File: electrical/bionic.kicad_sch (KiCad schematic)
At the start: 22 parts, among them J1 GPIO, U1 CAT24C256

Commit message: add(electrical/symbol): Updated Components
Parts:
- removed C1: 100n, symbol Device:C_Small
- removed D? (x4): TB6612, symbol Motor_Driver:TB6612_DC_Driver
- removed J1: GPIO, Connector_PinSocket_2.54mm:PinSocket_2x20_P2.54mm_Vertical, symbol Connector_Generic:Conn_02x20_Odd_Even
- removed JP1: ID_WP, symbol Jumper:SolderJumper_2_Open
- removed M? (x8): N20, symbol bionic:N20_EN
- removed R1, R2: 3.9k, symbol Device:R_Small
- removed U1: CAT24C256, symbol Memory_EEPROM:CAT24C256
- removed U?: MCP23017, symbol bionic:MCP23017
- removed U?: CD4069, symbol bionic:CD4069
- removed U?: ESP32, symbol bionic:ESP32
- removed U?: ADS1115, symbol bionic:ADS1115
- added D1, D2, D3, D4: TB6612, symbol bionic:TB6612
- added M1, M2, M3, M4, M5, M6, M7: N20, symbol bionic:N20_EN
- added U1: ESP32, symbol bionic:ESP32
- added U2: SAMD09, symbol bionic:SAMD09
- added U3, U4: CD4069, symbol bionic:CD4069
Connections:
- net +3V3: now also D1.13 (STBY), D1.2 (VCC), D2.13 (STBY), D2.2 (VCC), D3.13 (STBY), D3.2 (VCC), D4.13 (STBY), D4.2 (VCC), M1.2 (VCC/BLK), M2.2 (VCC/BLK), M3.2 (VCC/BLK), M4.2 (VCC/BLK), M5.2 (VCC/BLK), M6.2 (VCC/BLK), M7.2 (VCC/BLK), U1.16 (VIN), U2.24 (VIN), U3.14 (VDD), U4.14 (VDD)
- net +6V: now also D1.1 (VM), D2.1 (VM), D3.1 (VM), D4.1 (VM)
- net EMG1: now also U2.1 (*2)
- net EMG2: now also U2.2 (*3)
- net GND: now also D1.3 (GND), D1.8 (GND), D1.9 (GND), D2.3 (GND), D2.8 (GND), D2.9 (GND), D3.3 (GND), D3.8 (GND), D3.9 (GND), D4.3 (GND), D4.8 (GND), D4.9 (GND), M1.5 (GND/BLU), M2.5 (GND/BLU), M3.5 (GND/BLU), M4.5 (GND/BLU), M5.5 (GND/BLU), M6.5 (GND/BLU), M7.5 (GND/BLU), U1.17 (GND), U2.22 (GND), U3.7 (GND), U4.7 (GND)
- net M1+: now also D1.4 (A01), M1.1 (M+/RED)
- net M1-: now also D1.5 (A02), M1.6 (M-/WHT)
- net M1B: now also D1.15 (AI2), U3.2 (A*)
- net M2+: now also D1.6 (B01), M2.1 (M+/RED)
- net M2-: now also D1.7 (B02), M2.6 (M-/WHT)
- net M2B: now also D1.11 (BI2), U3.4 (B*)
- net M3+: now also D2.4 (A01), M3.1 (M+/RED)
- net M3-: now also D2.5 (A02), M3.6 (M-/WHT)
- net M3B: now also D2.15 (AI2), U3.6 (C*)
- net M4+: now also D2.6 (B01), M4.1 (M+/RED)
- net M4-: now also D2.7 (B02), M4.6 (M-/WHT)
- net M4B: now also D2.11 (BI2), U3.8 (D*)
- net M5+: now also D3.4 (A01), M5.1 (M+/RED)
- net M5-: now also D3.5 (A02), M5.6 (M-/WHT)
- net M5B: now also D3.15 (AI2), U3.10 (*E)
- net M6+: now also D3.6 (B01), M6.1 (M+/RED)
- net M6-: now also D3.7 (B02), M6.6 (M-/WHT)
- net M6B: now also D3.11 (BI2), U3.12 (*F)
- net M7+: now also D4.4 (A01), M7.1 (M+/RED)
- net M7-: now also D4.5 (A02), M7.6 (M-/WHT)
- net M7B: now also D4.15 (AI2), U4.2 (A*)
- new net DIR1: D1.14 (AI1), U2.4 (~5), U3.1 (A)
- new net DIR2: D1.12 (BI1), U2.5 (~6), U3.3 (B)
- new net DIR3: D2.14 (AI1), U2.6 (~7), U3.5 (C)
- new net DIR4: D2.12 (BI1), U2.8 (9), U3.9 (D)
- new net DIR5: D3.14 (AI1), U2.9 (10), U3.11 (E)
- new net DIR6: D3.12 (BI1), U2.10 (11), U3.13 (F)
- new net DIR7: D4.14 (AI1), U2.11 (14), U4.1 (A)
- new net EMG3: U2.3 (*4)
- new net ENA1: M1.3 (A/YLW), U1.10 (IO19)
- new net ENA2: M2.3 (A/YLW), U1.18 (IO13)
- new net ENA3: M3.3 (A/YLW), U1.20 (IO14)
- new net ENA4: M4.3 (A/YLW), U1.22 (IO26)
- new net ENA5: M5.3 (A/YLW), U1.24 (IO33)
- new net ENA6: M6.3 (A/YLW), U1.26 (IO35)
- new net ENA7: M7.3 (A/YLW), U1.28 (IO39/VN)
- new net ENB1: M1.4 (B/GRN), U1.15 (IO23)
- new net ENB2: M2.4 (B/GRN), U1.19 (IO12*)
- new net ENB3: M3.4 (B/GRN), U1.21 (IO27)
- new net ENB4: M4.4 (B/GRN), U1.23 (IO25)
- new net ENB5: M5.4 (B/GRN), U1.25 (IO32)
- new net ENB6: M6.4 (B/GRN), U1.27 (IO34)
- new net ENB7: M7.4 (B/GRN), U1.29 (IO36/VP)
- new net PWM1: D1.16 (PWMA), U1.3 (IO15*)
- new net PWM2: D1.10 (PWMB), U1.4 (IO2*)
- new net PWM3: D2.16 (PWMA), U1.5 (IO4)
- new net PWM4: D2.10 (PWMB), U1.6 (IO16/RX)
- new net PWM5: D3.16 (PWMA), U1.7 (IO17/TX)
- new net PWM6: D3.10 (PWMB), U1.8 (IO5*)
- new net PWM7: D4.16 (PWMA), U1.9 (IO18)
- new net SCL: U1.14 (IO22/SCL), U2.16 (SCL)
- new net SDA: U1.11 (IO21/SDA), U2.15 (SDA)
- no-connect marks 19 -> 28
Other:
- note removed: "ID_SD and ID_SC PINS: These pins are reserved for HAT ID EEPROM. At boot time this I2C interface will be interrogated to look for an EEPROM that identifes the attached board and allows automagic setup of the GPIOs (and optionally, Linux drivers). Bridging JP1 enables write protection. DO NOT USE these pins for anything other than attaching an I2C ID EEPROM. Leave unconnected if ID EEPROM not requ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"

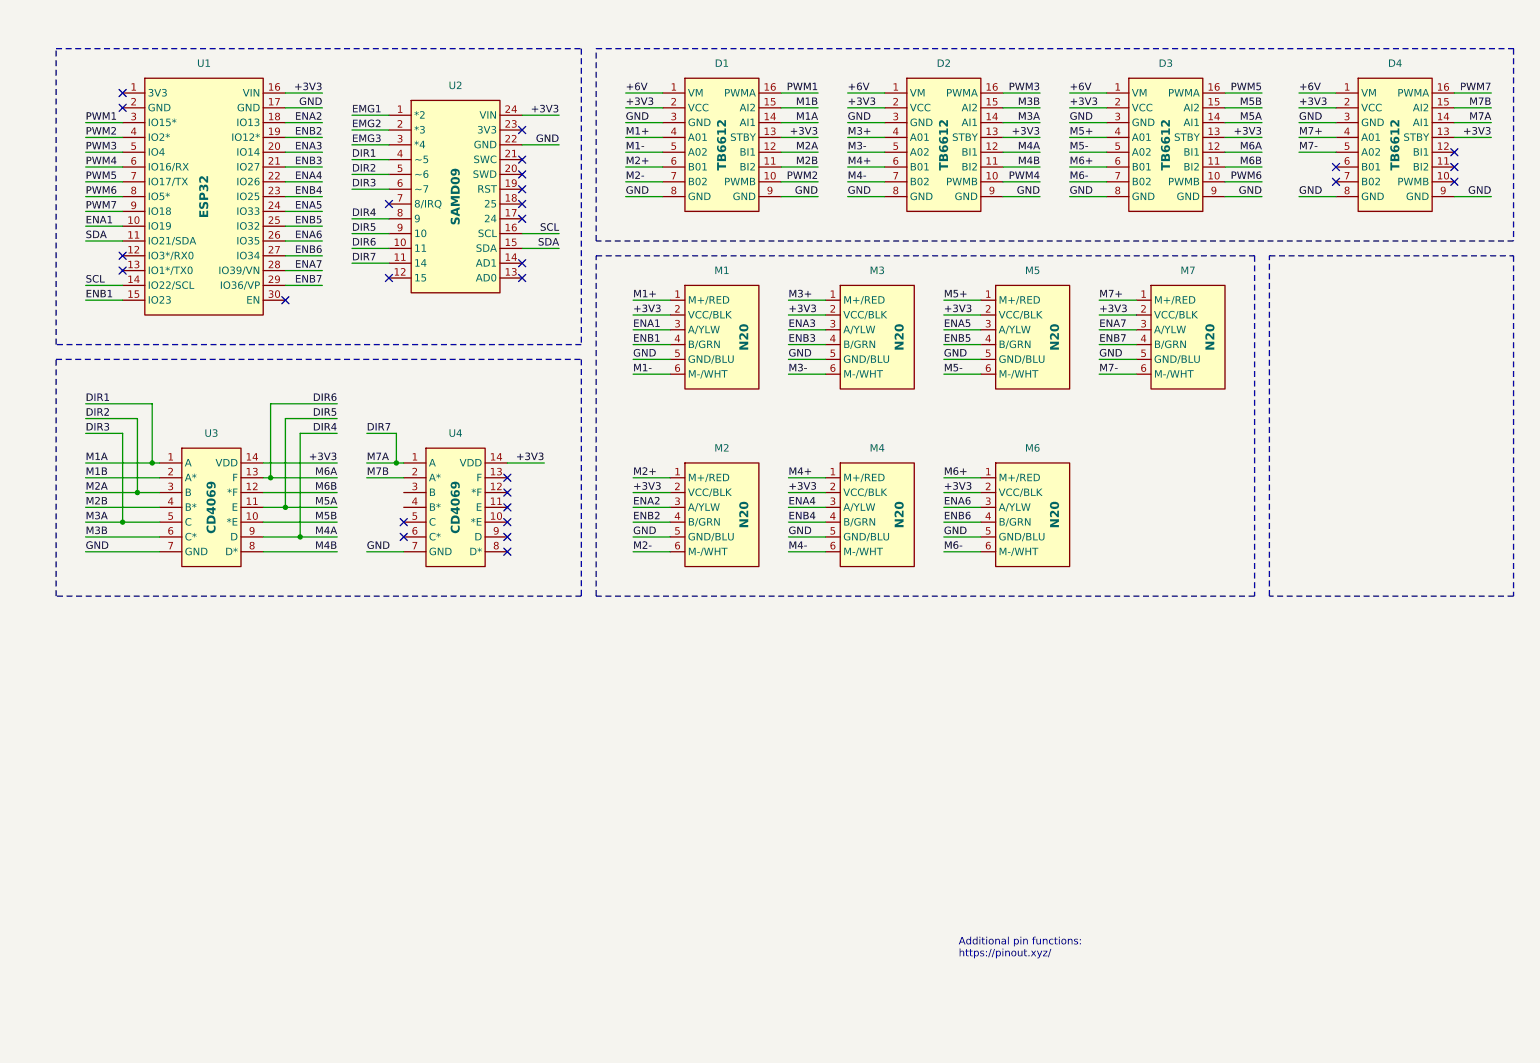
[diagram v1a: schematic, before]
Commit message: update(electrical): bionicBoard 'ERC Passed!'
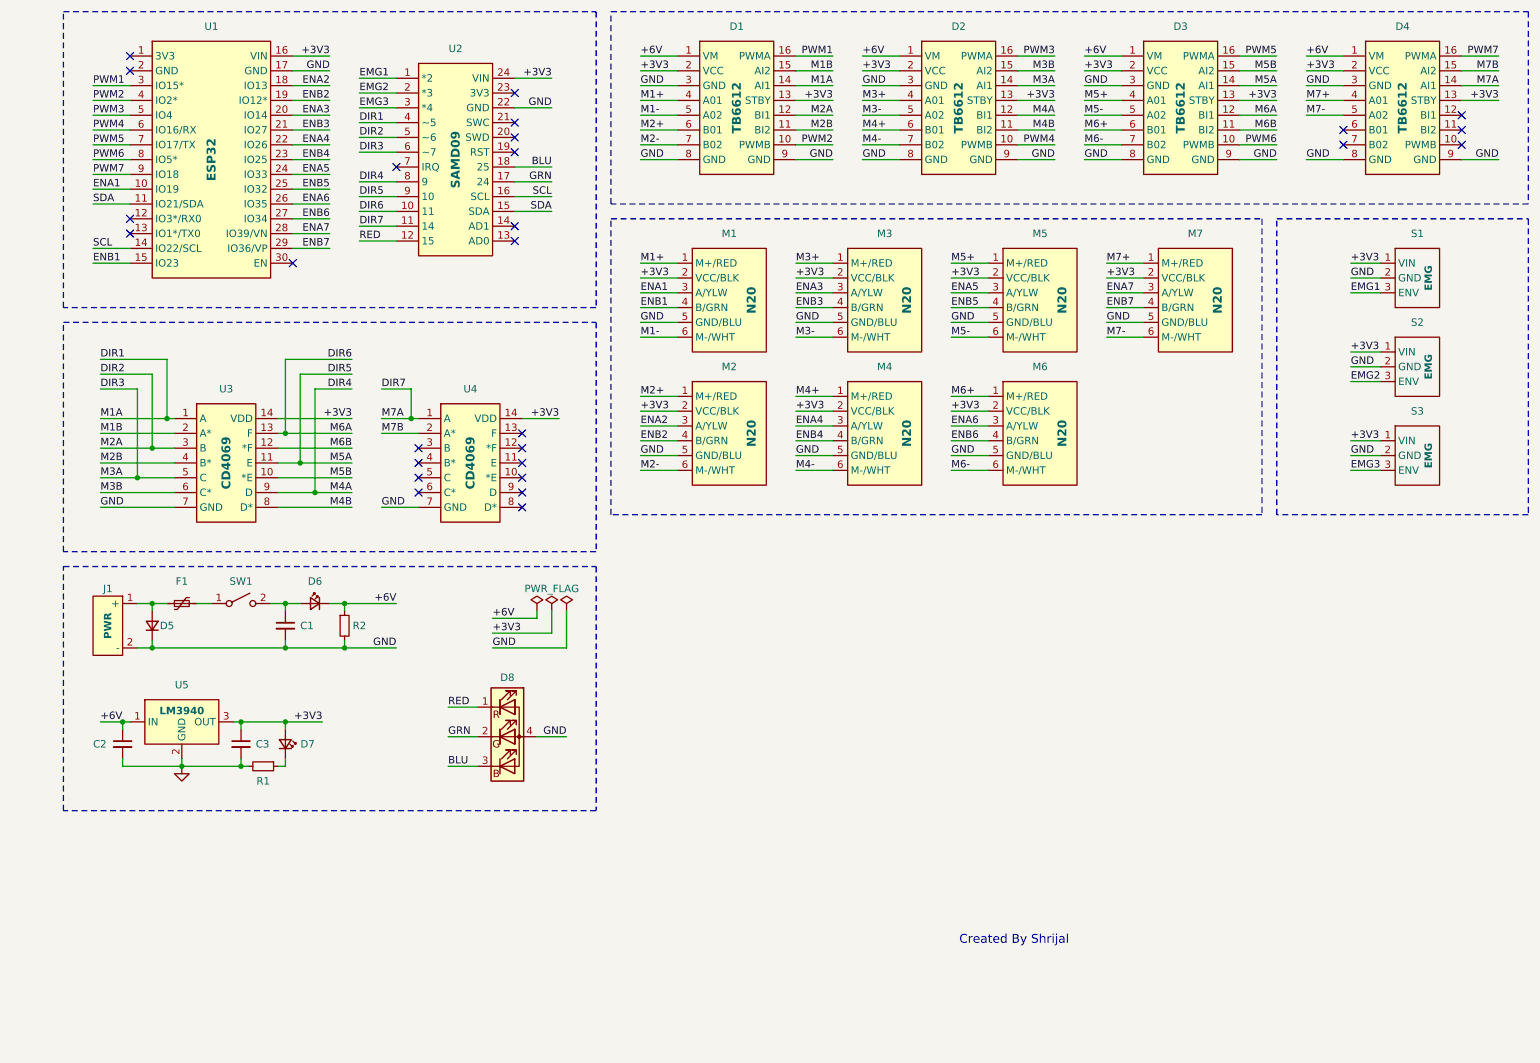
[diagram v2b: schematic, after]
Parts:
- added C1, C2, C3: C_Small, symbol Device:C_Small
- added D5: D_Small, symbol Device:D_Small
- added D6, D7: LED_Small, symbol Device:LED_Small
- added D8: LED_RGBA, symbol Device:LED_RGBA
- added F1: Polyfuse_Small, symbol Device:Polyfuse_Small
- added J1: PWR, symbol bionic:PWR
- added R1, R2: R_Small, symbol Device:R_Small
- added S1, S2, S3: EMG, symbol bionic:EMG
- added SW1: SW_SPST, symbol Switch:SW_SPST
- added U5: LM3940, symbol bionic:LM3940
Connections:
- net +3V3: now also C3.1, D7.2 (A), S1.1 (VIN), S2.1 (VIN), S3.1 (VIN), U5.3 (OUT)
- net +6V: now also C2.1, D6.1 (K), R2.1, U5.1 (IN)
- net EMG1: now also S1.3 (ENV)
- net EMG2: now also S2.3 (ENV)
- net EMG3: now also S3.3 (ENV)
- net GND: now also C1.2, C2.2, C3.2, D5.1 (K), D8.4 (A), J1.2 (-), R1.2, R2.2, S1.2 (GND), S2.2 (GND), S3.2 (GND), U5.2 (GND)
- net RED: now reaches U2.12 (15)
- net RED: now also D8.1 (RK)
- net GRN: now reaches U2.17 (24)
- net GRN: now also D8.2 (GK)
- net BLU: now reaches U2.18 (25)
- net BLU: now also D8.3 (BK)
- new net: C1.1, D6.2 (A), SW1.2 (B)
- new net: F1.2, SW1.1 (A)
- new net: D5.2 (A), F1.1, J1.1 (+)
- new net: D7.1 (K), R1.1
- no-connect marks 28 -> 27
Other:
- note added: "Created By Shrijal"
- note removed: "Additional pin functions: https://pinout.xyz/"
- company: (none) -> SERB Internship, NIT Patna
- title: (none) -> Bionic Arm Controller
- moved on the sheet: D1, D2, D3, D4, M1, M2, M3, M4, M5, M6, U1, U2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

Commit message: add(electrical/footprint): Updated Footprints
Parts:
- removed S3: EMG, symbol bionic:EMG
- added J2, J3: Screw_Terminal_01x02, Connector_PinHeader_2.54mm:PinHeader_1x02_P2.54mm_Vertical, symbol Connector:Screw_Terminal_01x02
- added S3: EMG1, symbol bionic:EMG1
- D1, D2, D3, D4: footprint (none) -> bionic:TB6612
- M1, M2, M3, M4, M5, M6, M7: footprint (none) -> Connector_PinHeader_2.54mm:PinHeader_1x06_P2.54mm_Vertical
- S1, S2: value EMG -> EMG2; footprint (none) -> Connector_PinHeader_2.54mm:PinHeader_1x03_P2.54mm_Vertical; symbol bionic:EMG -> bionic:EMG2
- U1: footprint (none) -> bionic:ESP32
- U2: footprint (none) -> bionic:SAMD09
- U3, U4: footprint (none) -> bionic:CD4069
- U5: footprint (none) -> Connector_PinHeader_2.54mm:PinHeader_1x03_P2.54mm_Vertical
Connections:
- net +3V3: now also J2.1 (Pin_1), S3.1 (+VS)
- net EMG3: now also S3.4 (SIG)
- net GND: now also J2.2 (Pin_2), J3.1 (Pin_1), S3.2 (GND), S3.5 (GND)
- new net -3V3: J3.2 (Pin_2), S3.3 (-VS)
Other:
- note removed: "Created By Shrijal"

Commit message: update(electrical): All Footprint Assigned!
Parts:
- removed J2, J3: Screw_Terminal_01x02, Connector_PinHeader_2.54mm:PinHeader_1x02_P2.54mm_Vertical, symbol Connector:Screw_Terminal_01x02
- removed S3: EMG1, symbol bionic:EMG1
- added H1, H2, H4: MountingHole_Pad, MountingHole:MountingHole_3.2mm_M3_Pad_Via, symbol Mechanical:MountingHole_Pad
- added H3: MountingHole, MountingHole:MountingHole_3.2mm_M3, symbol Mechanical:MountingHole
- added R2, R4: R_Small, Resistor_THT:R_Axial_DIN0207_L6.3mm_D2.5mm_P7.62mm_Horizontal, symbol Device:R_Small
- added RV1: R_Potentiometer_Small, Potentiometer_THT:Potentiometer_Runtron_RM-065_Vertical, symbol Device:R_Potentiometer_Small
- C1, C2, C3: footprint (none) -> Capacitor_THT:CP_Radial_D4.0mm_P2.00mm
- D5: footprint (none) -> Diode_THT:D_DO-35_SOD27_P7.62mm_Horizontal
- D6, D7: footprint (none) -> LED_THT:LED_D5.0mm
- D8: footprint (none) -> LED_THT:LED_D5.0mm-4_RGB
- F1: footprint (none) -> bionic:RGEF500
- J1: footprint (none) -> TerminalBlock_Phoenix:TerminalBlock_Phoenix_MKDS-1,5-2-5.08_1x02_P5.08mm_Horizontal; now in the parts list
- R1: renamed from R2; footprint (none) -> Resistor_THT:R_Axial_DIN0207_L6.3mm_D2.5mm_P7.62mm_Horizontal
- R3: renamed from R1; footprint (none) -> Resistor_THT:R_Axial_DIN0207_L6.3mm_D2.5mm_P7.62mm_Horizontal
- SW1: footprint (none) -> TerminalBlock_Phoenix:TerminalBlock_Phoenix_MKDS-1,5-2-5.08_1x02_P5.08mm_Horizontal
- U5: value LM3940 -> LM338; symbol bionic:LM3940 -> bionic:LM338
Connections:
- net +3V3: now also U5.2 (OUT), R2.1; no longer U5.3 (OUT)
- net +6V: now also D6.2 (A), U5.3 (IN); no longer D6.1 (K), U5.1 (IN)
- net DIR1: now also U2.8 (9); no longer U2.4 (~5)
- net DIR2: now also U2.9 (10); no longer U2.5 (~6)
- net DIR3: now also U2.10 (11), U4.1 (A); no longer U2.6 (~7), U3.5 (C)
- net DIR4: now also U2.11 (14), U4.3 (B); no longer U2.8 (9), U3.9 (D)
- net DIR5: now also U2.12 (15), U4.11 (E); no longer U2.9 (10), U3.11 (E)
- net DIR6: now also U2.17 (24), U4.13 (F); no longer U2.10 (11), U3.13 (F)
- net DIR7: now also D4.12 (BI1), U2.18 (25), U3.13 (F); no longer D4.14 (AI1), U2.11 (14), U4.1 (A)
- net ENA1: now also U1.23 (IO25); no longer U1.10 (IO19)
- net ENA2: now also U1.24 (IO33); no longer U1.18 (IO13)
- net ENA3: now also U1.26 (IO35); no longer U1.20 (IO14)
- net ENA4: now also U1.29 (IO36/VP); no longer U1.22 (IO26)
- net ENA5: now also U1.4 (IO2*); no longer U1.24 (IO33)
- net ENA6: now also U1.7 (IO17/TX); no longer U1.26 (IO35)
- net ENA7: now also U1.10 (IO19); no longer U1.28 (IO39/VN)
- net ENB1: now also U1.22 (IO26); no longer U1.15 (IO23)
- net ENB2: now also U1.25 (IO32); no longer U1.19 (IO12*)
- net ENB3: now also U1.27 (IO34); no longer U1.21 (IO27)
- net ENB4: now also U1.28 (IO39/VN); no longer U1.23 (IO25)
- net ENB5: now also U1.5 (IO4); no longer U1.25 (IO32)
- net ENB6: now also U1.8 (IO5*); no longer U1.27 (IO34)
- net ENB7: now also U1.15 (IO23); no longer U1.29 (IO36/VP)
- net GND: now also D5.2 (A), H1.1, H2.1, H4.1, R4.1, RV1.2; no longer D5.1 (K), D8.4 (A), U5.2 (GND)
- net M3B: now also U4.2 (A*); no longer U3.6 (C*)
- net M4B: now also U4.4 (B*); no longer U3.8 (D*)
- net M5B: now also U4.10 (*E); no longer U3.10 (*E)
- net M6B: now also U4.12 (*F); no longer U3.12 (*F)
- net M7+: now also D4.6 (B01); no longer D4.4 (A01)
- net M7-: now also D4.7 (B02); no longer D4.5 (A02)
- net M7B: now also D4.11 (BI2), U3.12 (*F); no longer D4.15 (AI2), U4.2 (A*)
- net PWM1: now also U1.18 (IO13); no longer U1.3 (IO15*)
- net PWM2: now also U1.19 (IO12*); no longer U1.4 (IO2*)
- net PWM3: now also U1.20 (IO14); no longer U1.5 (IO4)
- net PWM4: now also U1.21 (IO27); no longer U1.6 (IO16/RX)
- net PWM5: now also U1.3 (IO15*); no longer U1.7 (IO17/TX)
- net PWM6: now also U1.6 (IO16/RX); no longer U1.8 (IO5*)
- net PWM7: now also D4.10 (PWMB); no longer D4.16 (PWMA)
- net at C1.1, SW1.2 (B): now also D6.1 (K); no longer D6.2 (A)
- net at F1.1, J1.1 (+): now also D5.1 (K); no longer D5.2 (A)
- net BLU renamed L_BLU
- net L_BLU: now also U2.6 (~7); no longer U2.18 (25)
- net EMG3: no longer names the net of U2.3 (*4)
- net GRN renamed L_GRN
- net L_GRN: now also U2.5 (~6); no longer U2.17 (24)
- net RED renamed L_RED
- net L_RED: now also U2.4 (~5); no longer U2.12 (15)
- new net: D8.4 (A), R4.2
- new net: R2.2, RV1.1, U5.1 (ADJ)
- no-connect marks 27 -> 29
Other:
- moved on the sheet: C1, C2, C3, D5, D6, D7, D8, F1, R1, R3, S1, S2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
